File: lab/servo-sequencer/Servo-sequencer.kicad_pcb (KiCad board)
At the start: 2 copper layers, 104 x 84 mm, 15 parts, among them U1 atmega328p

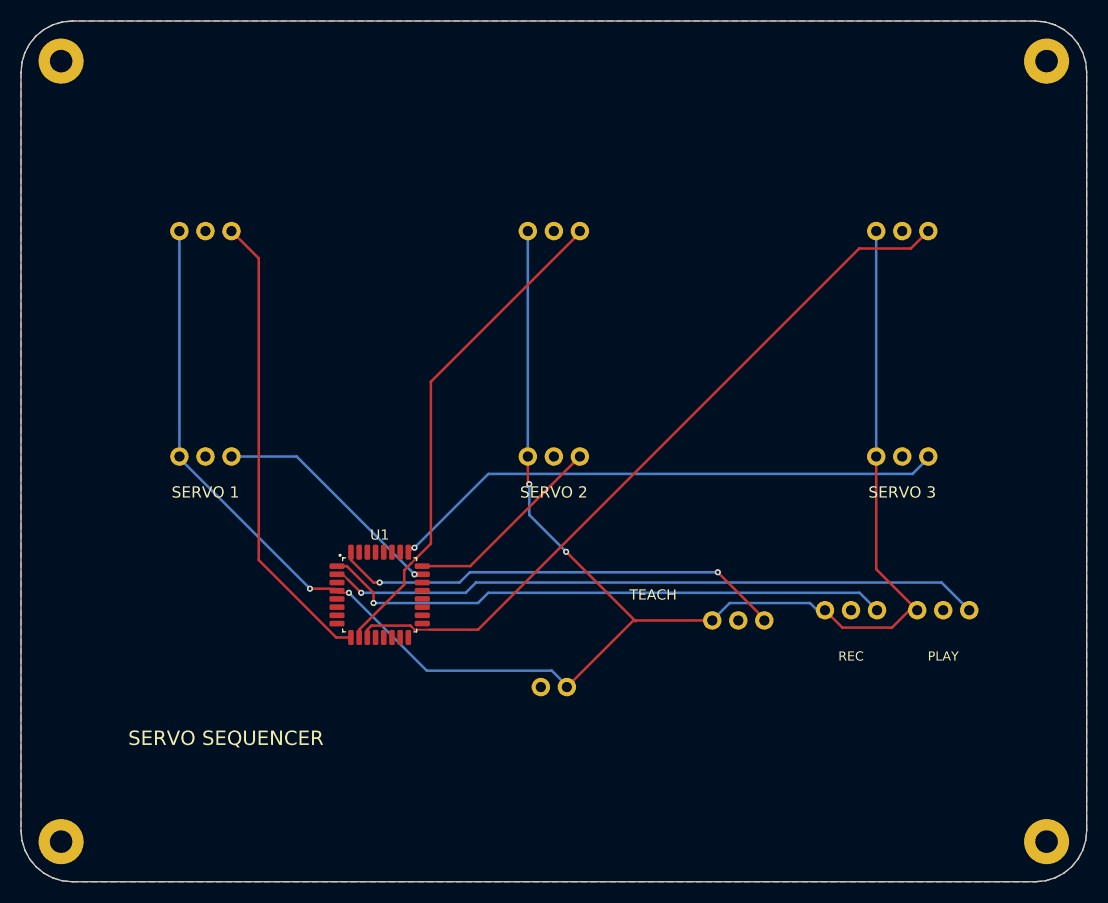
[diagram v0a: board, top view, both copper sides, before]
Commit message: lab: every board is a real board: an Arduino Nano and registry parts, routed, ready to order
The lab boards ran on simulation-only envelopes (labMcu, labDisplay, a battery). Now each is
an Arduino Nano on two sockets on the back (flashed over its USB, the image the app builds),
its lights LEDs through 1 kΩ, its knobs PTV09A pots, its display the MAX7219 eight-digit
module, its sensors an SHT31 and an SCD40 with their datasheets' support circuits, the FTDI
header for the serial console; the servo boards take 5 V on a screw terminal with a bulk
capacitor. All ten check complete with no errors or warnings, their firmware unchanged
(serial-device now on the 328P), and run in the lab without a fault (3 s each, dev host).

The registry: every interactive board must be ready to order and flash (publish.mjs refuses
one that is not; status simulation-only removed).

Claude-Session: https://claude.ai/code/session_01ATmMmxyrWxFwR3nTdXUrcx
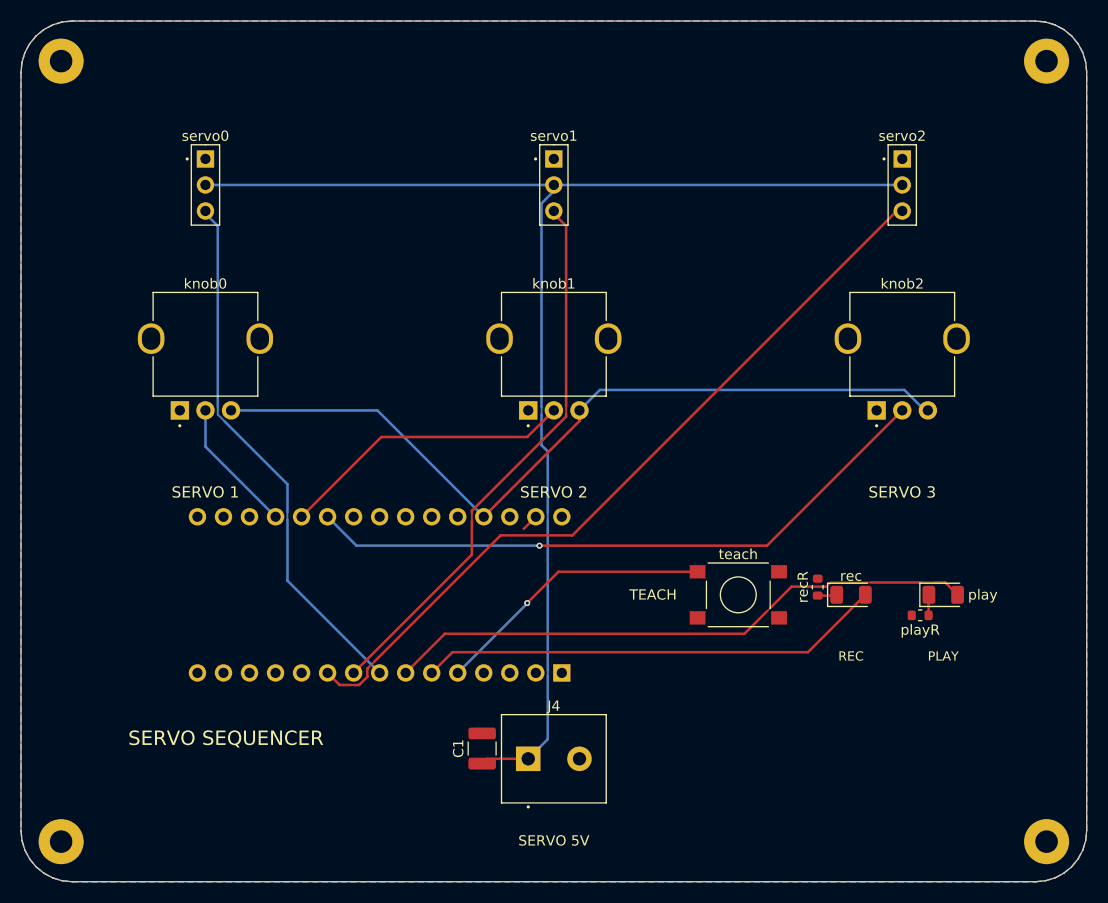
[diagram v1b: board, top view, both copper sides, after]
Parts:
- removed battery: battery, Regulated battery module
- removed the play at (190.0, 172.0)
- removed the rec at (181.0, 172.0)
- removed the teach at (170.0, 172.0)
- added C1: 100uF, C_1210_3225Metric, F.Cu at (145.0, 187.0)
- added J4: 5 V 2 A, TerminalBlock_1x02_P5.00mm, F.Cu at (152.0, 188.0)
- added play: green, LED_1206_3216Metric, F.Cu at (190.0, 172.0)
- added playR: 1kohm, R_0603_1608Metric, F.Cu at (187.8, 174.0)
- added rec: red, LED_1206_3216Metric, F.Cu at (181.0, 172.0)
- added recR: 1kohm, R_0603_1608Metric, F.Cu at (177.8, 171.2)
- added teach: PTS645SM43SMTR92 LFS, SW_Tactile_SPST_6x6mm_SMD, F.Cu at (170.0, 172.0)
- U1: value atmega328p -> A000005; footprint TQFP-32_7x7mm_P0.8mm -> Arduino_Nano_Socket_2x15_P2.54mm_W15.24mm; moved to B.Cu
- knob0, knob1, knob2: value potentiometer -> PTV09A-4020F-B103; footprint Potentiometer module -> Potentiometer_Bourns_PTV09A-4_Vertical
- servo0, servo1, servo2: value servo -> RC servo header, 1 x 3 pins, 2.54 mm; footprint Servo module -> PinHeader_1x03_P2.54mm_Vertical
- turned U1 to 90 degrees
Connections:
- U1 pad 1: REC -> (no net)
- U1 pad 10: SERVO1 -> SERVO2
- U1 pad 11: SERVO2 -> (no net)
- U1 pad 19: (no net) -> KNOB0
- U1 pad 2: PLAY -> (no net)
- U1 pad 20: (no net) -> KNOB1
- U1 pad 21: (no net) -> KNOB2
- U1 pad 23: KNOB0 -> (no net)
- U1 pad 24: KNOB1 -> (no net)
- U1 pad 25: KNOB2 -> (no net)
- U1 pad 27: (no net) -> V5
- U1 pad 29: (no net) -> GND
- U1 pad 3: GND -> (no net)
- U1 pad 4: V5 -> GND
- U1 pad 5: (no net) -> TEACH
- U1 pad 6: (no net) -> REC
- U1 pad 7: (no net) -> PLAY
- U1 pad 8: (no net) -> SERVO0
- U1 pad 9: SERVO0 -> SERVO1
- knob0 pad 1: V5 -> GND
- knob0 pad 2: GND -> KNOB0
- knob0 pad 3: KNOB0 -> V5
- knob1 pad 1: V5 -> GND
- knob1 pad 2: GND -> KNOB1
- knob1 pad 3: KNOB1 -> V5
- knob2 pad 1: V5 -> GND
- knob2 pad 2: GND -> KNOB2
- knob2 pad 3: KNOB2 -> V5
- servo0 pad 1: V5 -> GND
- servo0 pad 2: GND -> VSERVO
- servo1 pad 1: V5 -> GND
- servo1 pad 2: GND -> VSERVO
- servo2 pad 1: V5 -> GND
- servo2 pad 2: GND -> VSERVO
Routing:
- net VSERVO: track 0.00 -> 130.2 mm
- net V5: track 189.7 -> 78.9 mm, vias 4 -> 0
- net TEACH: track 44.5 -> 27.5 mm, vias 2 -> 1
- net KNOB0: track 24.1 -> 13.2 mm, vias 1 -> 0
- net REC: track 55.9 -> 45.5 mm, vias 1 -> 0
- net KNOB1: track 19.8 -> 28.9 mm
- net KNOB2: track 54.7 -> 62.7 mm
- net SERVO0: track 45.3 -> 52.1 mm
- net PLAY: track 64.0 -> 58.0 mm, vias 1 -> 0
- net SERVO1: track 48.6 -> 54.2 mm
- net SERVO2: track 71.9 -> 76.2 mm
- net PLAY_K: track 0.00 -> 2.01 mm
- net REC_K: track 0.00 -> 1.88 mm
- net GND: track 0.00 -> 1.68 mm
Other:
- board text added: "SERVO 5V"

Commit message: registry: every board rebuilt with pcbkit main 4684674e6 - the bought part named on the board
pcbkit dc07fdfd6 writes the bought row's MPN and Manufacturer (the design's own kept as DesignMPN /
DesignManufacturer) and the build chooses parts before it places (6361ec104). Each of the 44 boards
was rebuilt (; the two P4 boards  only: their builds reroute pairs):
copper unchanged on all 44 (segments, arcs and vias counted before and after), placement kept; the
Arduino and lab boards now carry the parts the catalogue gives them. The check gains only the new
judgements: part-maker (a part bought from another maker) and part-missing on hand-fitted modules
(DS1 sockets); p4-touch-7 loses part-stale. The P4 boards keep their hole-clearance errors (a
reroute is Team 3's).

Claude-Session: https://claude.ai/code/session_01BAgp959tApA8aEg85EYgfb
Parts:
- H1, H2, H3, H4: value (none) -> MountingHole_2.2mm_M2_Pad
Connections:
- teach pad 2: TEACH -> GND
